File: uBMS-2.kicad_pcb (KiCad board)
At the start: 4 copper layers, 60 x 90 mm, 183 parts, among them J1 Conn_02x03_Counter_Clockwise, J2 Conn_01x02, J3 Conn_01x01, J4 Conn_01x01, J5 Conn_02x07_Odd_Even, J6 Conn_02x07_Odd_Even, J7 Conn_02x07_Odd_Even, J8 Conn_01x01, Q1 2N7002, Q10 FQD5N20L, Q11 FQD5N20L, Q12 FQD5N20L, Q13 FQD5N20L, Q14 FQD5N20L, Q15 FQD5N20L, Q2 2N7002, Q3 NTD5865NL, Q4 FQD5N20L, Q5 FQD5N20L, Q6 FQD5N20L, Q7 FQD5N20L, Q8 FQD5N20L, Q9 FQD5N20L, U1 LM2576HVS-5, U10 CD74HC4067SM, U11 CD74HC4067SM, U2 ADS1115IDGS, U3 TLV1117-33, U4 TL431DBZ, U5 ESP32-WROOM-32, U6 TSC2012IDT, U7 MCP23017_SS, U8 MCP23008-E_P, U9 VDMG10C0

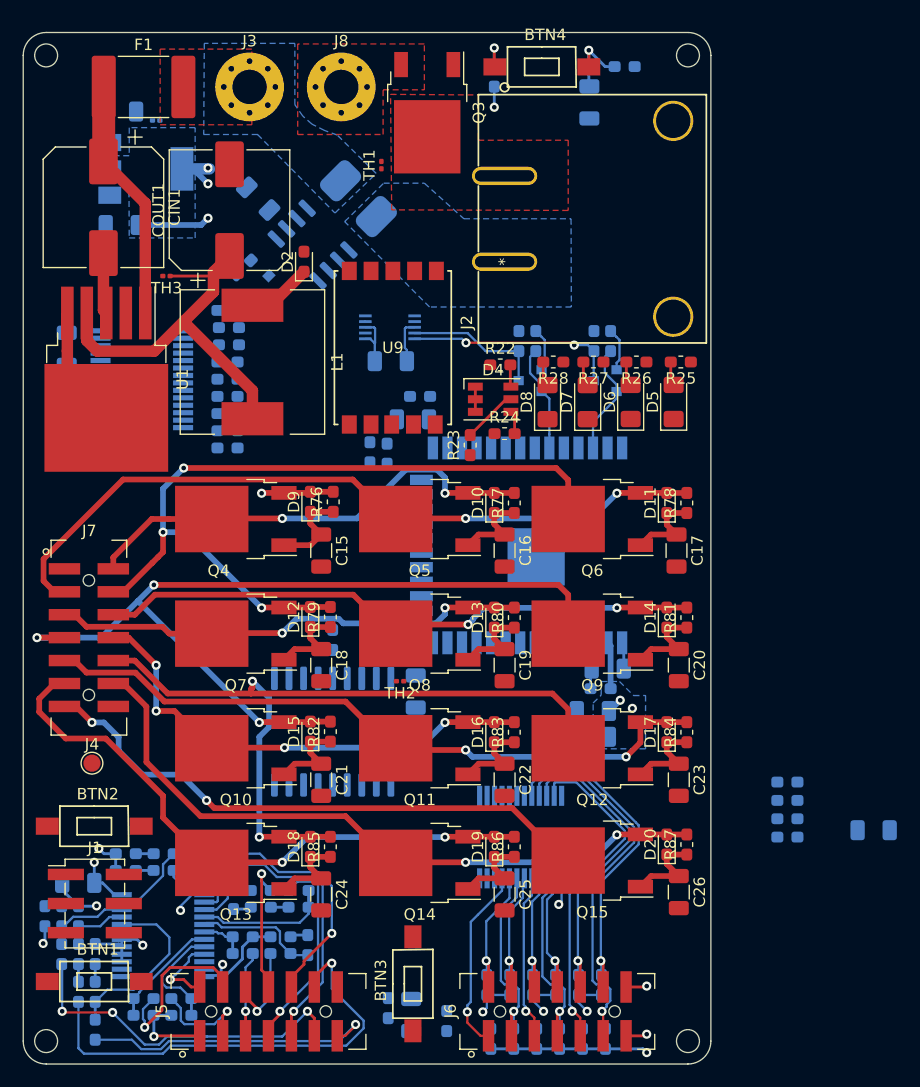
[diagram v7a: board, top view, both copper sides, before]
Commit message: Routed a LOT more PCB traces
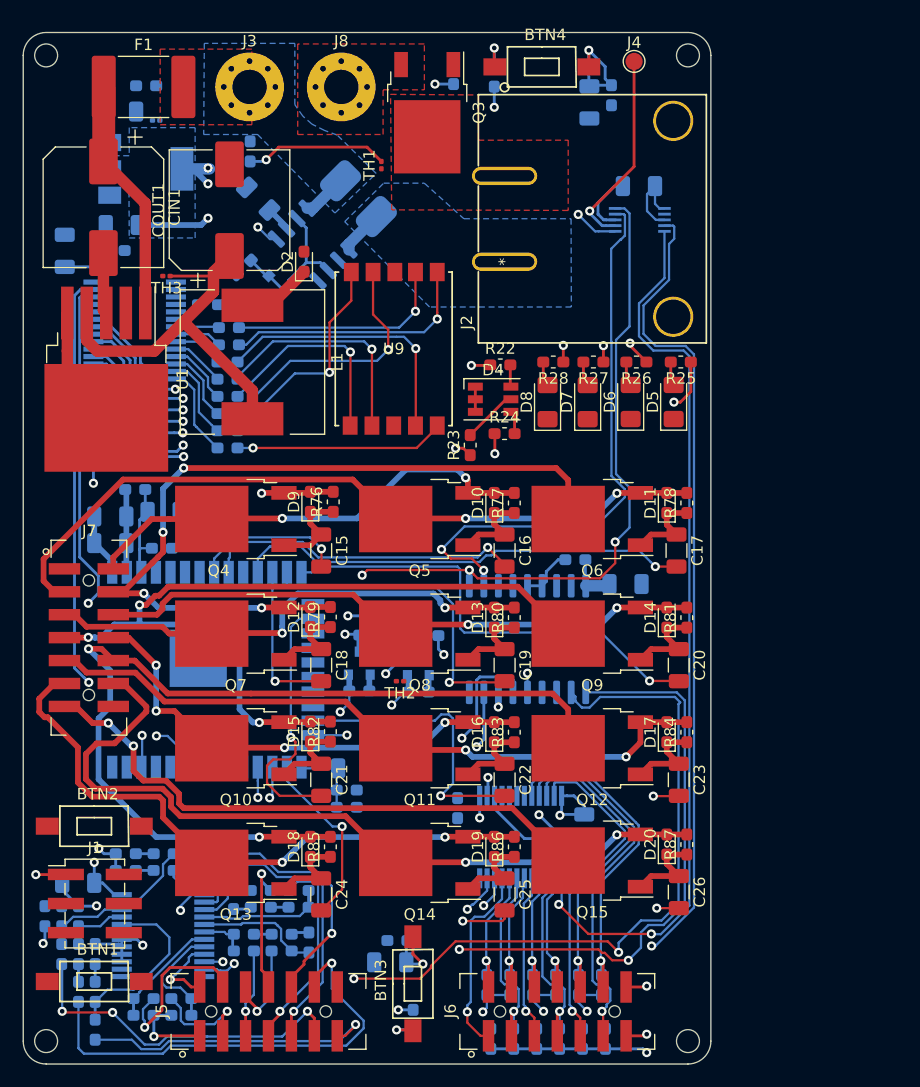
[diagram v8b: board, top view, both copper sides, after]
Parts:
- moved R75 86.2 mm to (30.7, 24.6)
- moved J4 77.4 mm to (73.3, 22.5)
- moved R74 76.8 mm to (28.0, 39.0)
- moved R72 72.3 mm to (39.8, 30.4), turned to 90 degrees
- moved R10 45.9 mm to (57.5, 23.6), turned to 270 degrees
- moved C3 45.4 mm to (27.6, 62.2)
- moved C2 45.4 mm to (27.6, 64.5)
- moved R3 44.2 mm to (29.8, 59.9), turned to 0 degrees
- moved C4 41.1 mm to (32.2, 61.8)
- moved R5 37.6 mm to (49.3, 77.5), turned to 180 degrees
- moved R4 34.9 mm to (48.2, 86.1), turned to 180 degrees
- moved Q2 32.7 mm to (49.3, 75.0), turned to 90 degrees
- moved R1 32.3 mm to (54.5, 77.5), turned to 180 degrees
- moved R6 32.3 mm to (50.2, 72.6), turned to 180 degrees
- moved D3 31.1 mm to (48.2, 87.6), turned to 180 degrees
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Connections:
- U2 pad 2: /ADC_Int -> Net-(U2-Pad2)
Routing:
- net /SDA_5V: track 12.3 -> 132.4 mm, vias 0 -> 4
- net /VoltageSense: track 2.90 -> 115.1 mm, vias 1 -> 2
- net /SCL_5V: track 18.7 -> 119.9 mm, vias 2 -> 5
- net /MOD_DSC_G: track 0.00 -> 79.3 mm, vias 0 -> 2
- net /TempSense: track 2.38 -> 79.0 mm, vias 1 -> 2
- net /S1_V: track 0.00 -> 74.9 mm, vias 0 -> 3
- net /S0_V: track 0.00 -> 72.3 mm, vias 0 -> 3
- net /LED_BAT_R: track 0.00 -> 64.1 mm, vias 0 -> 2
- net /LED_BAT_Y: track 0.00 -> 56.0 mm, vias 0 -> 2
- net /LED_BAT_G2: track 0.00 -> 53.5 mm, vias 0 -> 2
- net /LED_BAT_G1: track 0.00 -> 50.6 mm, vias 0 -> 2
- net +3V3: track 116.6 -> 163.0 mm
- net /PWM_Blnce_12: track 0.00 -> 44.3 mm, vias 0 -> 2
- net /LED_R: track 0.00 -> 44.1 mm, vias 0 -> 2
- net /LED_B: track 0.00 -> 42.4 mm, vias 0 -> 2
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- removed copper zone on In1.Cu, net GND
